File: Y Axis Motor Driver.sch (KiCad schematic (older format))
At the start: 36 parts

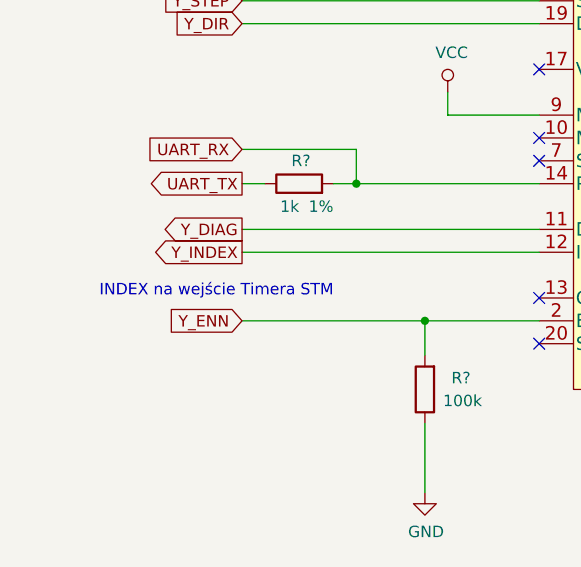
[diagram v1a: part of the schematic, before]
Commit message: Added Polyfuses and replace diodes
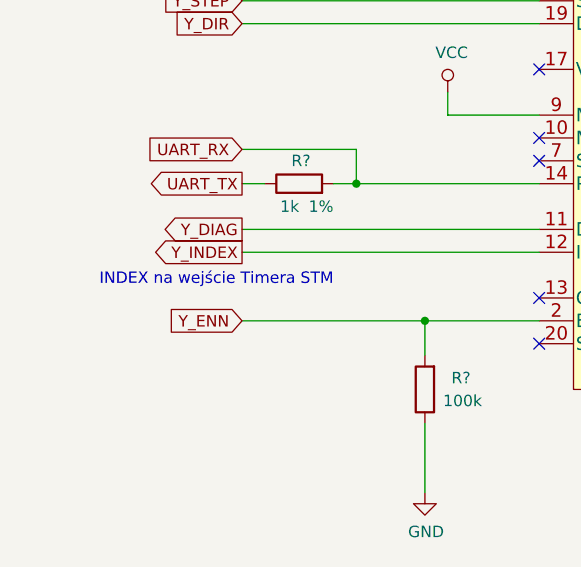
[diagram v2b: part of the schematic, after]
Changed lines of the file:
@@
 $Descr A4 11693 8268
 encoding utf-8
-Sheet 2 9
+Sheet 2 10
 Title "Y Axis Motor Driver"
 Date "2019-12-02"
@@
 Wire Wire Line
 	2900 4000 1600 4000
-Text Notes 2000 4300 2    50   ~ 0
+Text Notes 2000 4250 2    50   ~ 0
 INDEX na wejście Timera STM
 NoConn ~ 2900 4300

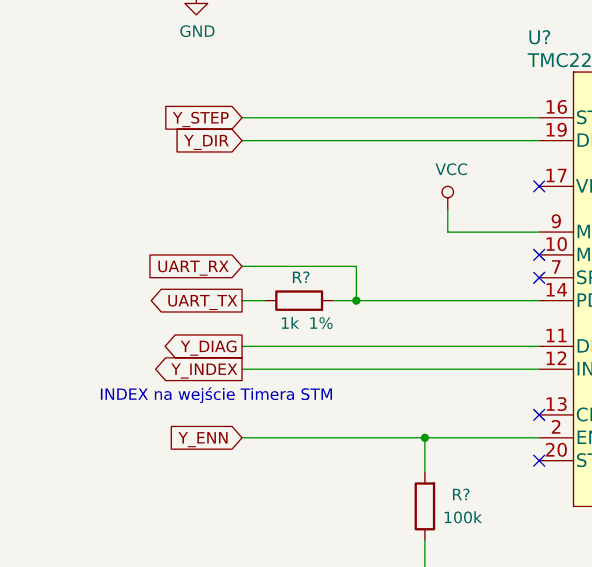
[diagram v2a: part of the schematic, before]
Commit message: Added USB B socket with ESD filter
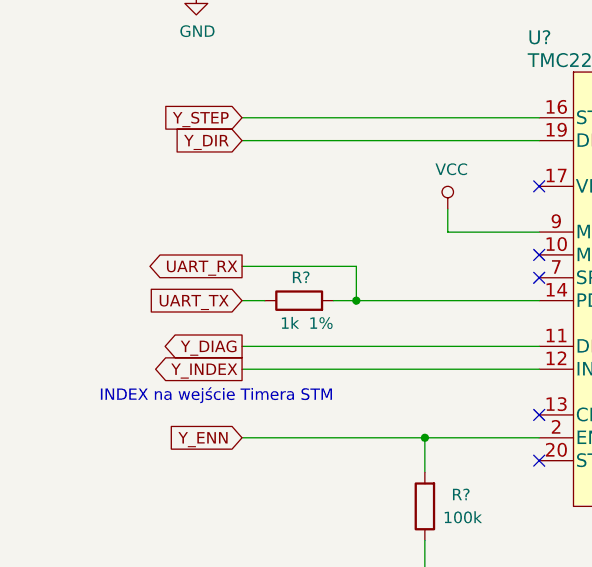
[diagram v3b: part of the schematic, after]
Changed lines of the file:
@@
 Text GLabel 1600 3100 0    50   Input ~ 0
 Y_DIR
-Text GLabel 1600 3650 0    50   Input ~ 0
-UART_RX
-Text GLabel 1600 3800 0    50   Output ~ 0
-UART_TX
 $Comp
 L Device:R R?
@@
 Wire Wire Line
 	2500 3500 2900 3500
+Text GLabel 1600 3800 0    50   Input ~ 0
+UART_TX
+Text GLabel 1600 3650 0    50   Output ~ 0
+UART_RX
 $EndSCHEMATC

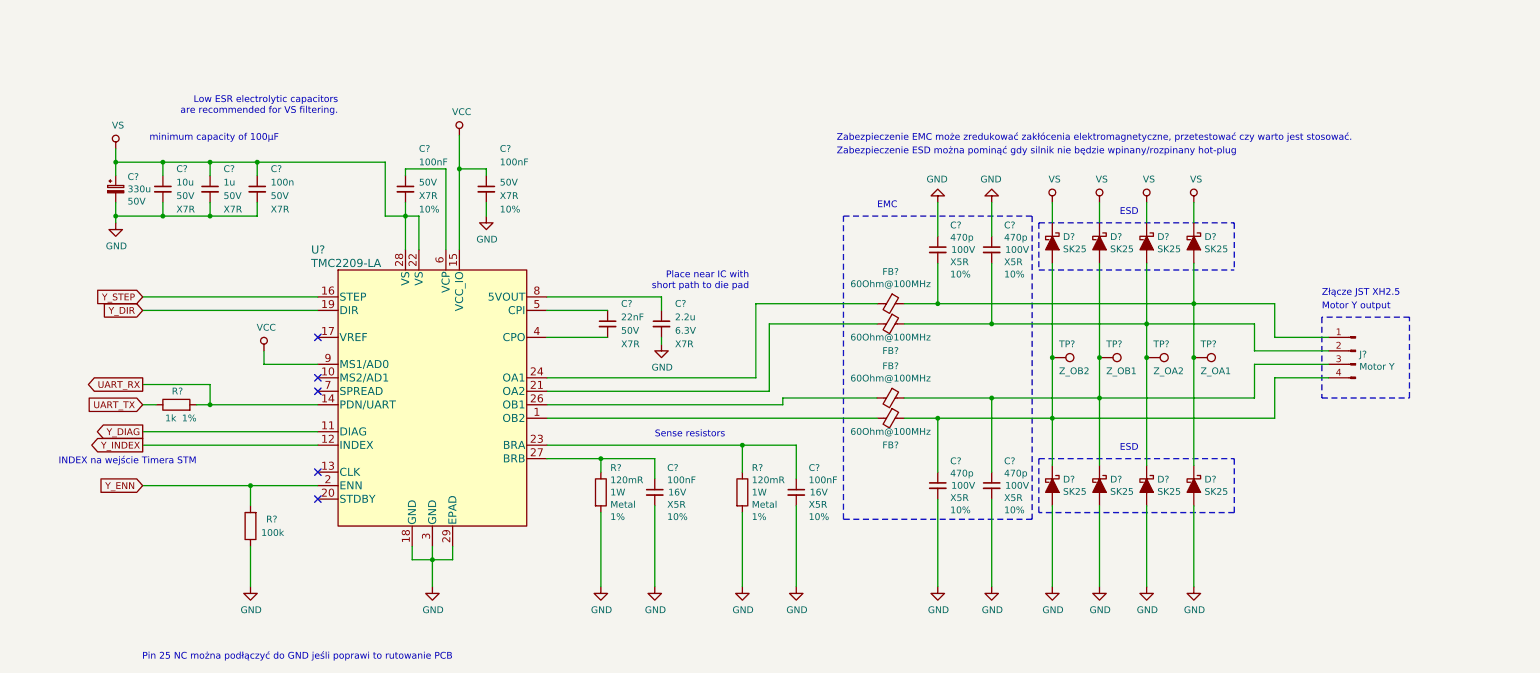
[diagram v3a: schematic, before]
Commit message: Numbering and finishing the schematic
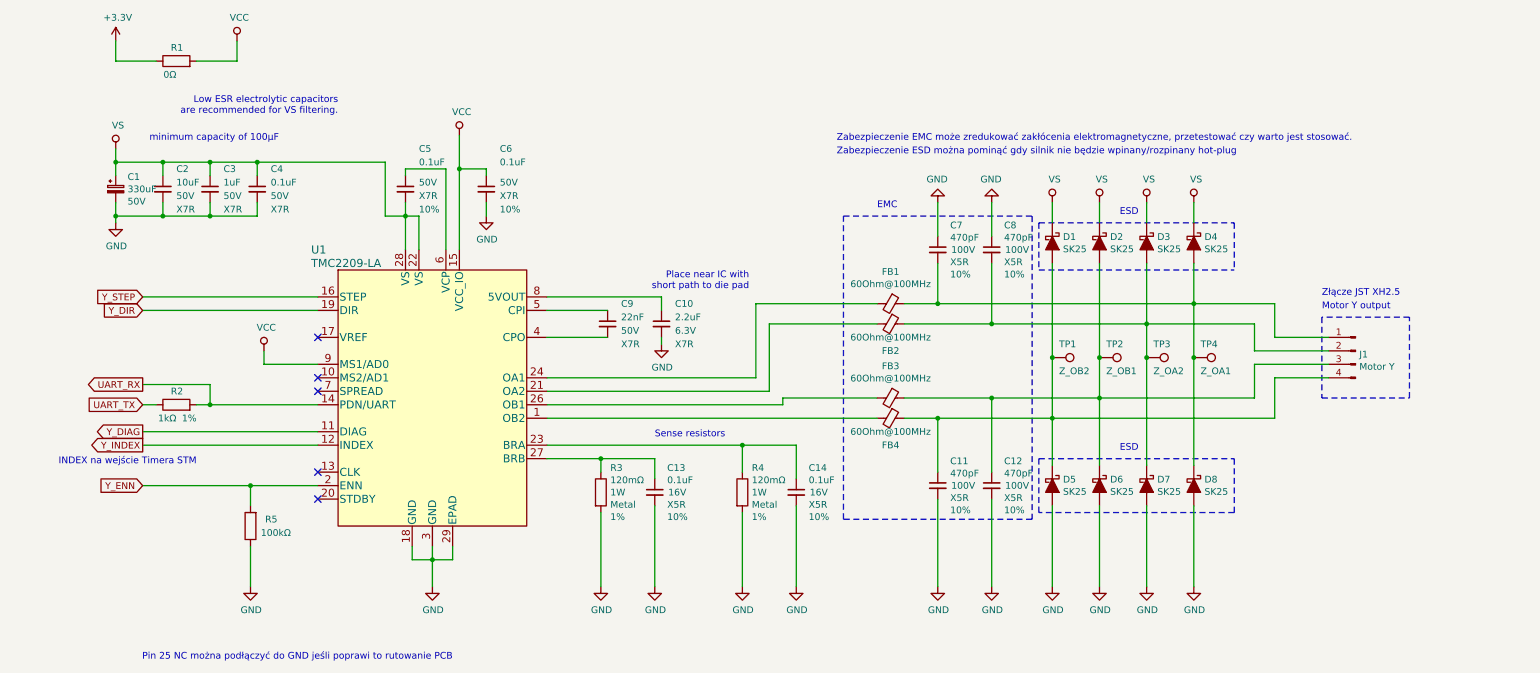
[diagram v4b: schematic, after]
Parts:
- added R1: 0Ω, Resistor_SMD:R_0805_2012Metric, symbol Device:R
- C1: renamed from C?; value 330u -> 330uF
- C10: renamed from C?; value 2.2u -> 2.2uF
- C11, C12, C7, C8: renamed from C?; value 470p -> 470pF
- C13, C14, C5, C6: renamed from C?; value 100nF -> 0.1uF
- C2: renamed from C?; value 10u -> 10uF
- C3: renamed from C?; value 1u -> 1uF
- C4: renamed from C?; value 100n -> 0.1uF
- R2: renamed from R?; value 1k -> 1kΩ
- R3, R4: renamed from R?; value 120mR -> 120mΩ
- R5: renamed from R?; value 100k -> 100kΩ
- gave numbers to parts that had none: 19
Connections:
- net VCC: now also R1.2
- new net +3V3: R1.1

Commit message: Shematic almost finished, BOM in KiCad 3/4 finished
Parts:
- C1: footprint (none) -> Capacitor_THT:CP_Radial_D10.0mm_P5.00mm; Cena (none) -> 0.6747; Model (none) -> ED1H331MNN1025; Producent (none) -> Elite; Tolerancja (none) -> 20%; Typ (none) -> THT
- C10: renamed from C14; Cena (none) -> 0.05982; Dielektryk X5R -> X7R; Model (none) -> CL10B104KB8NNNC; Napięcie 16V -> 50V; Producent (none) -> SAMSUNG; Typ (none) -> SMD
- C11: renamed from C7; footprint Capacitor_SMD:C_0603_1608Metric -> Capacitor_SMD:C_0805_2012Metric; Cena (none) -> 0.09147; Link (none) -> https://www.tme.eu/pl/details/c0805c471j1gac/kondensatory-m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; Model (none) -> C0805C471J1GAC; Producent (none) -> KEMET; Tolerancja 10% -> (none); Typ (none) -> SMD
- C12: renamed from C11; footprint Capacitor_SMD:C_0603_1608Metric -> Capacitor_SMD:C_0805_2012Metric; Cena (none) -> 0.09147; Link (none) -> https://www.tme.eu/pl/details/c0805c471j1gac/kondensatory-m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; Model (none) -> C0805C471J1GAC; Producent (none) -> KEMET; Tolerancja 10% -> (none); Typ (none) -> SMD
- C13: renamed from C8; footprint Capacitor_SMD:C_0603_1608Metric -> Capacitor_SMD:C_0805_2012Metric; Cena (none) -> 0.09147; Link (none) -> https://www.tme.eu/pl/details/c0805c471j1gac/kondensatory-m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; Model (none) -> C0805C471J1GAC; Producent (none) -> KEMET; Tolerancja 10% -> (none); Typ (none) -> SMD
- C14: renamed from C12; footprint Capacitor_SMD:C_0603_1608Metric -> Capacitor_SMD:C_0805_2012Metric; Cena (none) -> 0.09147; Link (none) -> https://www.tme.eu/pl/details/c0805c471j1gac/kondensatory-m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; Model (none) -> C0805C471J1GAC; Producent (none) -> KEMET; Tolerancja 10% -> (none); Typ (none) -> SMD
- C2: footprint (none) -> Capacitor_SMD:C_1210_3225Metric; Cena (none) -> 1.45250; Model (none) -> CL32B106KBJNNNE; Producent (none) -> SAMSUNG; Tolerancja (none) -> 10%; Typ (none) -> SMD
- C3: footprint (none) -> Capacitor_SMD:C_0805_2012Metric; Cena (none) -> 0.09; Model (none) -> CL21B105KBFNNNE; Producent (none) -> SAMSUNG; Tolerancja (none) -> 10%; Typ (none) -> SMD
- C4: Cena (none) -> 0.05982; Model (none) -> CL10B104KB8NNNC; Producent (none) -> SAMSUNG; Tolerancja (none) -> 10%; Typ (none) -> SMD
- C5, C6: Cena (none) -> 0.05982; Model (none) -> CL10B104KB8NNNC; Producent (none) -> SAMSUNG; Typ (none) -> SMD
- C7: renamed from C9; Cena (none) -> 0.07284; Link (none) -> https://www.tme.eu/pl/details/cc0603krx7r9223/kondensatory-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; Model (none) -> CC0603KRX7R9223; Producent (none) -> YAGEO; Tolerancja (none) -> 10%; Typ (none) -> SMD
- C8: renamed from C13; Cena (none) -> 0.05982; Dielektryk X5R -> X7R; Model (none) -> CL10B104KB8NNNC; Napięcie 16V -> 50V; Producent (none) -> SAMSUNG; Typ (none) -> SMD
- C9: renamed from C10; Cena (none) -> 0.08; Link (none) -> https://www.tme.eu/pl/details/cl10a225kp8nnnc/kondensatory-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; Model (none) -> CL10A225KP8NNNC; Producent (none) -> SAMSUNG; Typ (none) -> SMD
- D1, D8: Cena (none) -> 0.2445; Link (none) -> https://www.tme.eu/pl/details/sk25-dio/diody-schottky-smd/d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; Model (none) -> SK25; Opis (none) -> Dioda: prostownicza Schottky; SMD; 50V; 2A; SMB; Producent (none) -> DIOTEC SEMICONDUCTOR; Typ (none) -> SMD
- D2: renamed from D5; Cena (none) -> 0.2445; Link (none) -> https://www.tme.eu/pl/details/sk25-dio/diody-schottky-smd/d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; Model (none) -> SK25; Opis (none) -> Dioda: prostownicza Schottky; SMD; 50V; 2A; SMB; Producent (none) -> DIOTEC SEMICONDUCTOR; Typ (none) -> SMD
- D3: renamed from D2; Cena (none) -> 0.2445; Link (none) -> https://www.tme.eu/pl/details/sk25-dio/diody-schottky-smd/d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; Model (none) -> SK25; Opis (none) -> Dioda: prostownicza Schottky; SMD; 50V; 2A; SMB; Producent (none) -> DIOTEC SEMICONDUCTOR; Typ (none) -> SMD
- D4: renamed from D6; Cena (none) -> 0.2445; Link (none) -> https://www.tme.eu/pl/details/sk25-dio/diody-schottky-smd/d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; Model (none) -> SK25; Opis (none) -> Dioda: prostownicza Schottky; SMD; 50V; 2A; SMB; Producent (none) -> DIOTEC SEMICONDUCTOR; Typ (none) -> SMD
- D5: renamed from D3; Cena (none) -> 0.2445; Link (none) -> https://www.tme.eu/pl/details/sk25-dio/diody-schottky-smd/d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; Model (none) -> SK25; Opis (none) -> Dioda: prostownicza Schottky; SMD; 50V; 2A; SMB; Producent (none) -> DIOTEC SEMICONDUCTOR; Typ (none) -> SMD
- D6: renamed from D7; Cena (none) -> 0.2445; Link (none) -> https://www.tme.eu/pl/details/sk25-dio/diody-schottky-smd/d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; Model (none) -> SK25; Opis (none) -> Dioda: prostownicza Schottky; SMD; 50V; 2A; SMB; Producent (none) -> DIOTEC SEMICONDUCTOR; Typ (none) -> SMD
- D7: renamed from D4; Cena (none) -> 0.2445; Link (none) -> https://www.tme.eu/pl/details/sk25-dio/diody-schottky-smd/d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; Model (none) -> SK25; Opis (none) -> Dioda: prostownicza Schottky; SMD; 50V; 2A; SMB; Producent (none) -> DIOTEC SEMICONDUCTOR; Typ (none) -> SMD
- TP1, TP2, TP3, TP4: footprint (none) -> TestPoint:TestPoint_Pad_D1.5mm
- U1: Cena (none) -> 10.30; Link (none) -> https://pl.farnell.com/trinamic/tmc2209-la-t/motor-driver-s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; Model (none) -> TMC2209-LA-T; Opis (none) -> Sterownik/kontroler silnika krokowego, 4.75V do 29V, 2A/1 w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; Producent (none) -> TRINAMIC; Typ (none) -> SMD
- renumbered R5 to R3, R3 to R4, R4 to R5

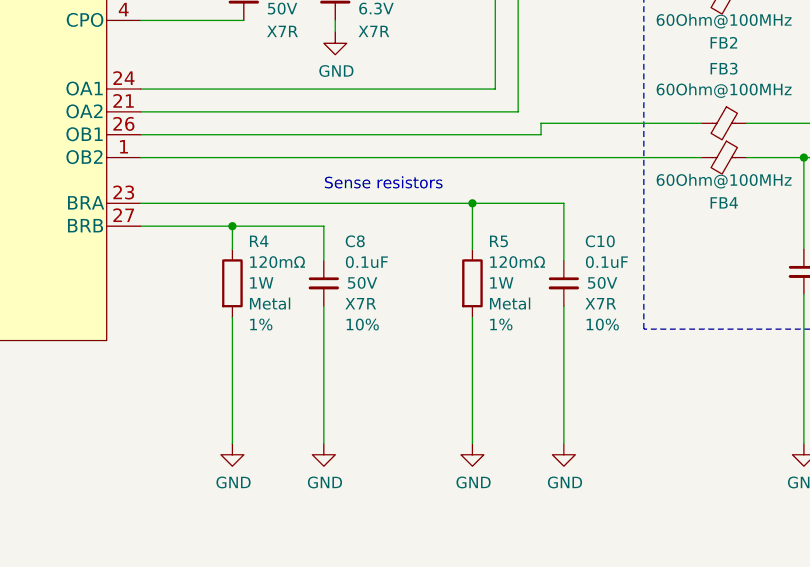
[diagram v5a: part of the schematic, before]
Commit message: BOM in KiCad almost finished, genereated NETLIST, create PCB
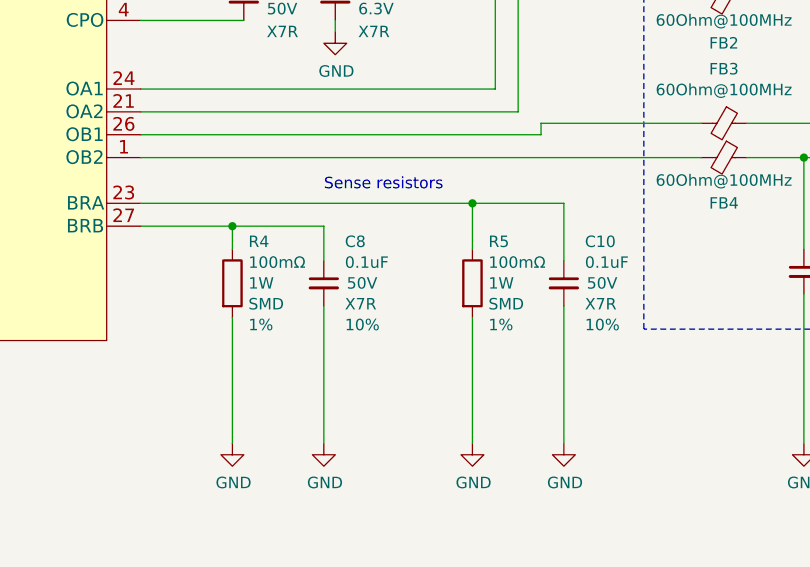
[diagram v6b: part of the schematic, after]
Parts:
- FB1, FB2, FB3, FB4: Cena (none) -> 0.13674; Link (none) -> https://www.tme.eu/pl/details/blm21pg600sn1d/ferryty-korali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; Opis (none) -> Ferryt: koralik; Imp.@ 100MHz: 60Ω; Montaż: SMD; 3A; Obud: 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; Producent (none) -> MURATA; Typ (none) -> SMD
- J1: Cena (none) -> 0.81567; Link (none) -> https://www.tme.eu/pl/details/b4b-xh-a/zlacza-sygnalowe-ras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; Model (none) -> B4B-XH-A; Opis (none) -> Gniazdo; przewód-płytka; męskie; XH; 2,5mm; PIN: 4; THT; 25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; Producent (none) -> JST; Typ (none) -> THT
- R1, R3: Cena (none) -> 0.04651; Typ (none) -> SMD
- R2: Cena (none) -> 0.04651; Link (none) -> https://www.tme.eu/pl/details/smd0603-1k-1%25/rezystory-smd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; Model (none) -> 0603SAF1001T5E; Opis (none) -> Rezystor: thick film; SMD; 0603; 1kΩ; 0,1W; ±1%; -55÷155°C; Producent (none) -> ROYAL OHM; Typ (none) -> SMD
- R4, R5: value 120mΩ -> 100mΩ; Cena (none) -> 0.76246; Link (none) -> https://www.tme.eu/pl/details/cs2010-0r1-1%25-hp/rezystory-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; Model (none) -> CS10FTFTR100; Opis (none) -> Rezystor: thick film; pomiarowy; SMD; 2010; 100mΩ; 1W; ±1%; Producent (none) -> VIKING; Typ Metal -> SMD
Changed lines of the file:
@@
 AR Path="/5DE587B9/5E249033" Ref="R4"  Part="1"
 F 0 "R4" H 5070 4632 50  0000 L CNN
-F 1 "120mΩ" H 5070 4541 50  0000 L CNN
+F 1 "100mΩ" H 5070 4541 50  0000 L CNN
 F 2 "Resistor_SMD:R_2010_5025Metric" V 4930 4450 50  0001 C CNN
 F 3 "~" H 5000 4450 50  0001 C CNN
 F 4 "1W" H 5070 4450 50  0000 L CNN "Moc"
-F 5 "Metal" H 5070 4359 50  0000 L CNN "Typ"
+F 5 "SMD" H 5070 4359 50  0000 L CNN "Typ"
 F 6 "1%" H 5070 4268 50  0000 L CNN "Tolerancja"
-F 7 "" H 5000 4450 50  0001 C CNN "Model"
+F 7 "CS10FTFTR100" H 5000 4450 50  0001 C CNN "Model"
+F 8 "0.76246" H 5000 4450 50  0001 C CNN "Cena"
+F 9 "https://www.tme.eu/pl/details/cs2010-0r1-1%25-hp/rezystory-smd-2010/viking/cs10ftftr100/" H 5000 4450 50  0001 C CNN "Link"
+F 10 "Rezystor: thick film; pomiarowy; SMD; 2010; 100mΩ; 1W; ±1%" H 5000 4450 50  0001 C CNN "Opis"
+F 11 "VIKING" H 5000 4450 50  0001 C CNN "Producent"
 	1    5000 4450
 	1    0    0    -1
@@
 AR Path="/5DE587B9/5E24905B" Ref="R5"  Part="1"
 F 0 "R5" H 6120 4632 50  0000 L CNN
-F 1 "120mΩ" H 6120 4541 50  0000 L CNN
+F 1 "100mΩ" H 6120 4541 50  0000 L CNN
 F 2 "Resistor_SMD:R_2010_5025Metric" V 5980 4450 50  0001 C CNN
 F 3 "~" H 6050 4450 50  0001 C CNN
 F 4 "1W" H 6120 4450 50  0000 L CNN "Moc"
-F 5 "Metal" H 6120 4359 50  0000 L CNN "Typ"
+F 5 "SMD" H 6120 4359 50  0000 L CNN "Typ"
 F 6 "1%" H 6120 4268 50  0000 L CNN "Tolerancja"
-F 7 "" H 6050 4450 50  0001 C CNN "Model"
+F 7 "CS10FTFTR100" H 6050 4450 50  0001 C CNN "Model"
+F 8 "0.76246" H 6050 4450 50  0001 C CNN "Cena"
+F 9 "https://www.tme.eu/pl/details/cs2010-0r1-1%25-hp/rezystory-smd-2010/viking/cs10ftftr100/" H 6050 4450 50  0001 C CNN "Link"
+F 10 "Rezystor: thick film; pomiarowy; SMD; 2010; 100mΩ; 1W; ±1%" H 6050 4450 50  0001 C CNN "Opis"
+F 11 "VIKING" H 6050 4450 50  0001 C CNN "Producent"
 	1    6050 4450
 	1    0    0    -1
@@
 F 3 "~" H 7150 3050 50  0001 C CNN
 F 4 "BLM21PG600SN1D" V 7150 3050 50  0001 C CNN "Model"
+F 5 "0.13674" H 7150 3050 50  0001 C CNN "Cena"
+F 6 "https://www.tme.eu/pl/details/blm21pg600sn1d/ferryty-koraliki/murata/" H 7150 3050 50  0001 C CNN "Link"
+F 7 "Ferryt: koralik; Imp.@ 100MHz: 60Ω; Montaż: SMD; 3A; Obud: 0805" H 7150 3050 50  0001 C CNN "Opis"
+F 8 "MURATA" H 7150 3050 50  0001 C CNN "Producent"
+F 9 "SMD" H 7150 3050 50  0001 C CNN "Typ"
 	1    7150 3050
 	0    1    1    0
@@
 F 3 "~" H 7150 3200 50  0001 C CNN
 F 4 "BLM21PG600SN1D" V 7150 3200 50  0001 C CNN "Model"
+F 5 "0.13674" H 7150 3200 50  0001 C CNN "Cena"
+F 6 "https://www.tme.eu/pl/details/blm21pg600sn1d/ferryty-koraliki/murata/" H 7150 3200 50  0001 C CNN "Link"
+F 7 "Ferryt: koralik; Imp.@ 100MHz: 60Ω; Montaż: SMD; 3A; Obud: 0805" H 7150 3200 50  0001 C CNN "Opis"
+F 8 "MURATA" H 7150 3200 50  0001 C CNN "Producent"
+F 9 "SMD" H 7150 3200 50  0001 C CNN "Typ"
 	1    7150 3200
 	0    1    1    0
@@
 F 3 "~" H 7150 3750 50  0001 C CNN
 F 4 "BLM21PG600SN1D" V 7150 3750 50  0001 C CNN "Model"
+F 5 "0.13674" H 7150 3750 50  0001 C CNN "Cena"
+F 6 "https://www.tme.eu/pl/details/blm21pg600sn1d/ferryty-koraliki/murata/" H 7150 3750 50  0001 C CNN "Link"
+F 7 "Ferryt: koralik; Imp.@ 100MHz: 60Ω; Montaż: SMD; 3A; Obud: 0805" H 7150 3750 50  0001 C CNN "Opis"
+F 8 "MURATA" H 7150 3750 50  0001 C CNN "Producent"
+F 9 "SMD" H 7150 3750 50  0001 C CNN "Typ"
 	1    7150 3750
 	0    1    1    0
@@
 F 3 "~" H 7150 3900 50  0001 C CNN
 F 4 "BLM21PG600SN1D" V 7150 3900 50  0001 C CNN "Model"
+F 5 "0.13674" H 7150 3900 50  0001 C CNN "Cena"
+F 6 "https://www.tme.eu/pl/details/blm21pg600sn1d/ferryty-koraliki/murata/" H 7150 3900 50  0001 C CNN "Link"
+F 7 "Ferryt: koralik; Imp.@ 100MHz: 60Ω; Montaż: SMD; 3A; Obud: 0805" H 7150 3900 50  0001 C CNN "Opis"
+F 8 "MURATA" H 7150 3900 50  0001 C CNN "Producent"
+F 9 "SMD" H 7150 3900 50  0001 C CNN "Typ"
 	1    7150 3900
 	0    1    1    0
@@
 F 2 "Connector_JST:JST_XH_B4B-XH-AM_1x04_P2.50mm_Vertical" H 10600 3400 50  0001 C CNN
 F 3 "~" H 10600 3400 50  0001 C CNN
+F 4 "0.81567" H 10600 3400 50  0001 C CNN "Cena"
+F 5 "https://www.tme.eu/pl/details/b4b-xh-a/zlacza-sygnalowe-raster-2-50mm/jst/" H 10600 3400 50  0001 C CNN "Link"
+F 6 "B4B-XH-A" H 10600 3400 50  0001 C CNN "Model"
+F 7 "Gniazdo; przewód-płytka; męskie; XH; 2,5mm; PIN: 4; THT; 250V; 3A" H 10600 3400 50  0001 C CNN "Opis"
+F 8 "JST" H 10600 3400 50  0001 C CNN "Producent"
+F 9 "THT" H 10600 3400 50  0001 C CNN "Typ"
 	1    10600 3400
 	-1   0    0    -1
@@
 F 3 "~" H 2400 4700 50  0001 C CNN
 F 4 "" H 2400 4700 50  0001 C CNN "Model"
+F 5 "0.04651" H 2400 4700 50  0001 C CNN "Cena"
+F 6 "SMD" H 2400 4700 50  0001 C CNN "Typ"
 	1    2400 4700
 	-1   0    0    1
@@
 F 3 "~" H 1850 3800 50  0001 C CNN
 F 4 "1%" V 1750 3650 50  0000 L CNN "Tolerancja"
-F 5 "" H 1850 3800 50  0001 C CNN "Model"
+F 5 "0603SAF1001T5E" H 1850 3800 50  0001 C CNN "Model"
+F 6 "0.04651" H 1850 3800 50  0001 C CNN "Cena"
+F 7 "https://www.tme.eu/pl/details/smd0603-1k-1%25/rezystory-smd-0603/royal-ohm/0603saf1001t5e/" H 1850 3800 50  0001 C CNN "Link"
+F 8 "Rezystor: thick film; SMD; 0603; 1kΩ; 0,1W; ±1%; -55÷155°C" H 1850 3800 50  0001 C CNN "Opis"
+F 9 "ROYAL OHM" H 1850 3800 50  0001 C CNN "Producent"
+F 10 "SMD" H 1850 3800 50  0001 C CNN "Typ"
 	1    1850 3800
 	0    -1   -1   0
@@
 F 4 "1%" V 1750 1100 50  0001 L CNN "Tolerancja"
 F 5 "" H 1850 1250 50  0001 C CNN "Model"
+F 6 "0.04651" H 1850 1250 50  0001 C CNN "Cena"
+F 7 "SMD" H 1850 1250 50  0001 C CNN "Typ"
 	1    1850 1250
 	0    -1   -1   0
